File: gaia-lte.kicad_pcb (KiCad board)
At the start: 6 copper layers, 50 x 50 mm, 49 parts, among them J1 4G antenna connector(U.FL), J2 AUX Ant connector(u.fl), J4 Micro_SD_Card_Det2, J5 SIM8051-6-0-14-00-A_REVD6, J6 Conn_02x10_Odd_Even, J7 Conn_02x10_Odd_Even, Q1 DTC143ZEBTL, Q2 DTC143ZEBTL, Q3 DTC143ZEBTL, Q4 DTC143ZEBTL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

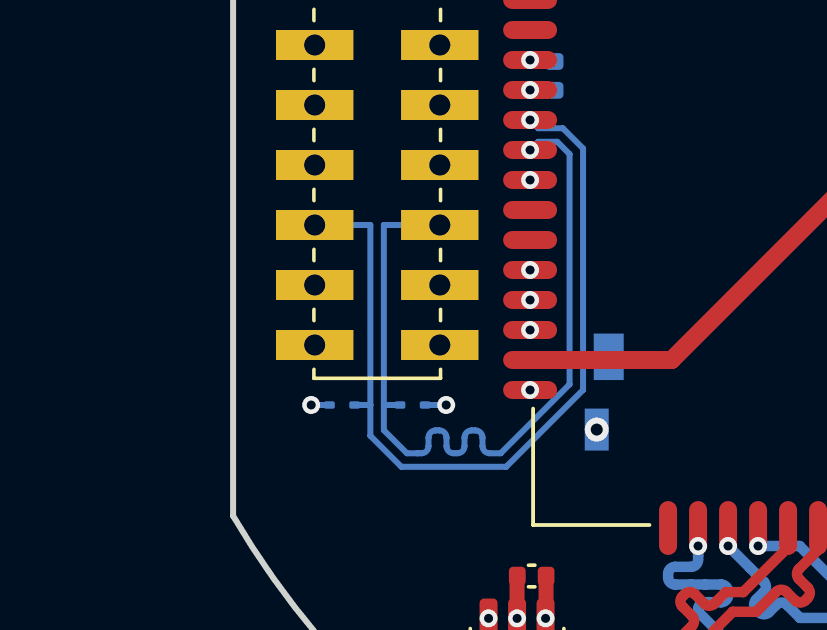
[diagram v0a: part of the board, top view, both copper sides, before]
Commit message: fixing 3d models
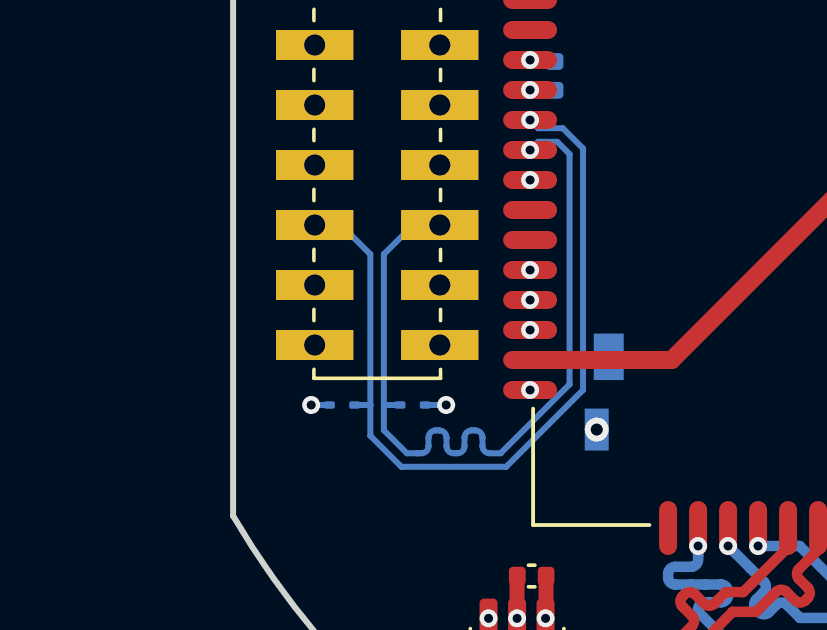
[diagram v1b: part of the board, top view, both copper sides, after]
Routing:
- net /USB_DN: track 28.1 -> 27.6 mm
- net /USB_DP: track 28.1 -> 27.6 mm
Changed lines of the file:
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@@
 			(remove_unused_layers yes)
 			(keep_end_layers yes)
-			(zone_layer_connections "In1.Cu" "In4.Cu")
+			(zone_layer_connections)
 			(net 1 "GND")
 			(pinfunction "Pin_8")
@@
 			(remove_unused_layers yes)
 			(keep_end_layers yes)
-			(zone_layer_connections "In1.Cu" "In4.Cu")
+			(zone_layer_connections)
 			(net 1 "GND")
 			(pinfunction "Pin_10")
@@
 			(remove_unused_layers yes)
 			(keep_end_layers yes)
-			(zone_layer_connections "In1.Cu" "In4.Cu")
+			(zone_layer_connections)
 			(net 1 "GND")
 			(pinfunction "Pin_17")
@@
 			(remove_unused_layers yes)
 			(keep_end_layers yes)
-			(zone_layer_connections "In1.Cu" "In4.Cu")
+			(zone_layer_connections)
 			(net 1 "GND")
 			(pinfunction "Pin_18")
@@
 			(remove_unused_layers yes)
 			(keep_end_layers yes)
-			(zone_layer_connections "In1.Cu" "In4.Cu")
+			(zone_layer_connections)
 			(net 1 "GND")
 			(pinfunction "Pin_19")
@@
 			(remove_unused_layers yes)
 			(keep_end_layers yes)
-			(zone_layer_connections "In1.Cu" "In4.Cu")
+			(zone_layer_connections)
 			(net 1 "GND")
 			(pinfunction "Pin_20")
@@
 		(model "${KICAD9_3DMODEL_DIR}/Connector_PinHeader_2.00mm.3dshapes/PinHeader_2x10_P2.00mm_Vertical_SMD.step"
 			(offset
-				(xyz 0 0 0)
+				(xyz 0 0 -0.8)
 			)
 			(scale
@@
 			)
 			(rotate
-				(xyz 0 0 0)
+				(xyz -0 -180 -0)
+			)
+		)
+		(model "${KIPRJMOD}/3dmodels/HDR2.00-F-LS-2X10P.step"
+			(offset
+				(xyz 0 9 0)
+			)
+			(scale
+				(xyz 1 1 1)
+			)
+			(rotate
+				(xyz -0 -0 -90)
 			)
 		)
@@
 			(remove_unused_layers yes)
 			(keep_end_layers yes)
-			(zone_layer_connections "In2.Cu")
+			(zone_layer_connections)
 			(net 67 "VBUS")
 			(pinfunction "Pin_3")
@@
 			(remove_unused_layers yes)
 			(keep_end_layers yes)
-			(zone_layer_connections "In1.Cu" "In4.Cu")
+			(zone_layer_connections)
 			(net 1 "GND")
 			(pinfunction "Pin_13")
@@
 			(remove_unused_layers yes)
 			(keep_end_layers yes)
-			(zone_layer_connections "In1.Cu" "In4.Cu")
+			(zone_layer_connections)
 			(net 1 "GND")
 			(pinfunction "Pin_14")
@@
 			(remove_unused_layers yes)
 			(keep_end_layers yes)
-			(zone_layer_connections "In1.Cu" "In4.Cu")
+			(zone_layer_connections)
 			(net 1 "GND")
 			(pinfunction "Pin_15")
@@
 			(remove_unused_layers yes)
 			(keep_end_layers yes)
-			(zone_layer_connections "In1.Cu" "In4.Cu")
+			(zone_layer_connections)
 			(net 1 "GND")
 			(pinfunction "Pin_16")
@@
 		(model "${KICAD9_3DMODEL_DIR}/Connector_PinHeader_2.00mm.3dshapes/PinHeader_2x10_P2.00mm_Vertical_SMD.step"
 			(offset
-				(xyz 0 0 0)
+				(xyz 0 0 -0.8)
 			)
 			(scale
@@
 			)
 			(rotate
-				(xyz 0 0 0)
+				(xyz -0 -180 -0)
+			)
+		)
+		(model "${KIPRJMOD}/3dmodels/HDR2.00-F-LS-2X10P.step"
+			(offset
+				(xyz 0 9 0)
+			)
+			(scale
+				(xyz 1 1 1)
+			)
+			(rotate
+				(xyz -0 -0 -90)
 			)
 		)
@@
 		)
 		(embedded_fonts no)
+		(model "${KIPRJMOD/3dmodels/SIM8051-6-0-14-00-A_REVD6.step"
+			(offset
+				(xyz 0 0 0)
+			)
+			(scale
+				(xyz 1 1 1)
+			)
+			(rotate
+				(xyz -90 -0 -0)
+			)
+		)
 	)
 	(gr_poly
@@
 	)
 	(segment
-		(start 169.222 96.5)
-		(end 171.086938 96.5)
-		(width 0.2)
-		(layer "B.Cu")
-		(net 8)
-	)
-	(segment
 		(start 175.001803 93.725001)
 		(end 175.412 94.135198)
@@
 	)
 	(segment
+		(start 169.222 102.5)
+		(end 169.222 97.474938)
+		(width 0.2)
+		(layer "B.Cu")
+		(net 8)
+	)
+	(segment
 		(start 175.412 94.135198)
 		(end 175.412 101.811802)
@@
 	)
 	(segment
-		(start 169.222 102.5)
-		(end 169.222 96.5)
+		(start 174.371937 93.725001)
+		(end 175.001803 93.725001)
 		(width 0.2)
 		(layer "B.Cu")
@@
 	)
 	(segment
-		(start 174.371937 93.725001)
-		(end 175.001803 93.725001)
+		(start 170.196938 96.5)
+		(end 171.086938 96.5)
 		(width 0.2)
 		(layer "B.Cu")
@@
 	)
 	(segment
+		(start 169.222 97.474938)
+		(end 170.196938 96.5)
+		(width 0.2)
+		(layer "B.Cu")
+		(net 8)
+	)
+	(segment
 		(start 175.412 101.811802)
 		(end 173.113802 104.11)
@@
 	)
 	(segment
-		(start 168.772 96.5)
-		(end 166.916938 96.5)
-		(width 0.2)
-		(layer "B.Cu")
-		(net 9)
-	)
-	(segment
 		(start 173.300198 104.56)
 		(end 169.804802 104.56)
@@
 	)
 	(segment
-		(start 174.096938 93)
-		(end 174.371937 93.274999)
+		(start 167.796938 96.5)
+		(end 166.916938 96.5)
 		(width 0.2)
 		(layer "B.Cu")
@@
 	)
 	(segment
-		(start 169.804802 104.56)
-		(end 168.772 103.527198)
+		(start 174.096938 93)
+		(end 174.371937 93.274999)
 		(width 0.2)
 		(layer "B.Cu")
@@
 	)
 	(segment
-		(start 168.772 102.5)
-		(end 168.772 96.5)
+		(start 169.804802 104.56)
+		(end 168.772 103.527198)
 		(width 0.2)
 		(layer "B.Cu")
@@
 		(width 0.2)
 		(layer "B.Cu")
+		(net 9)
+	)
+	(segment
+		(start 168.772 102.5)
+		(end 168.772 97.475062)
+		(width 0.2)
+		(layer "B.Cu")
+		(net 9)
+	)
+	(segment
+		(start 168.772 97.475062)
+		(end 167.796938 96.5)
+		(width 0.2)
+		(layer "B.Cu")

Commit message: header fix
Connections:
- J6 pad 6: unconnected-(J6-Pin_6-Pad6) -> GND
- J6 pad 9: unconnected-(J6-Pin_9-Pad9) -> GND

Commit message: v1.1 - PROD
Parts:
- added R5: 22, Resistor_SMD:R_0402_1005Metric, B.Cu at (175.9, 96.3)
- added R6: 22, Resistor_SMD:R_0402_1005Metric, B.Cu at (174.9, 96.3)
- moved D7 0.20 mm to (170.4, 102.5)
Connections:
- U3 pad 12: /USB_DN -> Net-(U3-USB_DN)
- U3 pad 13: /USB_DP -> Net-(U3-USB_DP)
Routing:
- net /USB_DN: track 27.6 -> 22.9 mm, vias 1 -> 0
- net /USB_DP: track 27.6 -> 23.4 mm, vias 1 -> 0
- net Net-(U3-USB_DN): track 0.00 -> 3.62 mm, vias 0 -> 1
- net Net-(U3-USB_DP): track 0.00 -> 2.38 mm, vias 0 -> 1
- net GND: track 57.8 -> 56.8 mm
- net /SD_DAT1: track 10.6 -> 9.82 mm
- net /SD_DAT0: track 9.83 -> 9.13 mm
- net /SD_CMD: track 9.82 -> 9.14 mm
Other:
- board text added: "revision 1.1 Project Neptune"
- board text removed: "revision 1.0"
